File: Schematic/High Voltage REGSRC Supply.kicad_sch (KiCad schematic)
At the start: 10 parts, among them Q17 BSS123

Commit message: added sensors?
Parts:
- renumbered C30 to C32, C31 to C33, C32 to C34, C33 to C35, Q17 to Q21

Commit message: 1st Schematic Review
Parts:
- renumbered C32 to C35, C33 to C36, C34 to C37, C35 to C38, R67 to R69, R68 to R70, R69 to R71, R70 to R72
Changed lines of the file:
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@@
 		(on_board yes)
 		(dnp no)
-		(property "Reference" "#PWR027"
+		(property "Reference" "#PWR032"
 			(at 129.54 104.14 0)
 			(effects
@@
 			(project "STAR"
 				(path "/fc8533bc-25dd-4c20-9b4c-ffebebd6739b/e8da5d81-614b-4fe5-84b3-4c351fab7114/e3d465d4-4bae-42f2-91c8-f61f15aa6ae9"
-					(reference "#PWR027")
+					(reference "#PWR032")
 					(unit 1)
 				)
@@
 		(on_board yes)
 		(dnp no)
-		(property "Reference" "#PWR028"
+		(property "Reference" "#PWR033"
 			(at 152.4 125.73 0)
 			(effects
@@
 			(project "STAR"
 				(path "/fc8533bc-25dd-4c20-9b4c-ffebebd6739b/e8da5d81-614b-4fe5-84b3-4c351fab7114/e3d465d4-4bae-42f2-91c8-f61f15aa6ae9"
-					(reference "#PWR028")
+					(reference "#PWR033")
 					(unit 1)
 				)
@@
 		(on_board yes)
 		(dnp no)
-		(property "Reference" "C33"
+		(property "Reference" "C36"
 			(at 129.54 90.932 0)
 			(effects
@@
 			(project "STAR"
 				(path "/fc8533bc-25dd-4c20-9b4c-ffebebd6739b/e8da5d81-614b-4fe5-84b3-4c351fab7114/e3d465d4-4bae-42f2-91c8-f61f15aa6ae9"
-					(reference "C33")
+					(reference "C36")
 					(unit 1)
 				)
@@
 		(on_board yes)
 		(dnp no)
-		(property "Reference" "R69"
+		(property "Reference" "R71"
 			(at 148.082 81.534 0)
 			(effects
@@
 			(project "STAR"
 				(path "/fc8533bc-25dd-4c20-9b4c-ffebebd6739b/e8da5d81-614b-4fe5-84b3-4c351fab7114/e3d465d4-4bae-42f2-91c8-f61f15aa6ae9"
-					(reference "R69")
+					(reference "R71")
 					(unit 1)
 				)
@@
 		(on_board yes)
 		(dnp no)
-		(property "Reference" "R68"
+		(property "Reference" "R70"
 			(at 144.272 95.504 0)
 			(effects
@@
 			(project "STAR"
 				(path "/fc8533bc-25dd-4c20-9b4c-ffebebd6739b/e8da5d81-614b-4fe5-84b3-4c351fab7114/e3d465d4-4bae-42f2-91c8-f61f15aa6ae9"
-					(reference "R68")
+					(reference "R70")
 					(unit 1)
 				)
@@
 		(on_board yes)
 		(dnp no)
-		(property "Reference" "C32"
+		(property "Reference" "C35"
 			(at 129.54 82.042 0)
 			(effects
@@
 			(project "STAR"
 				(path "/fc8533bc-25dd-4c20-9b4c-ffebebd6739b/e8da5d81-614b-4fe5-84b3-4c351fab7114/e3d465d4-4bae-42f2-91c8-f61f15aa6ae9"
-					(reference "C32")
+					(reference "C35")
 					(unit 1)
 				)
@@
 		(on_board yes)
 		(dnp no)
-		(property "Reference" "C34"
+		(property "Reference" "C37"
 			(at 152.4 112.522 0)
 			(effects
@@
 			(project "STAR"
 				(path "/fc8533bc-25dd-4c20-9b4c-ffebebd6739b/e8da5d81-614b-4fe5-84b3-4c351fab7114/e3d465d4-4bae-42f2-91c8-f61f15aa6ae9"
-					(reference "C34")
+					(reference "C37")
 					(unit 1)
 				)
@@
 		(on_board yes)
 		(dnp no)
-		(property "Reference" "C35"
+		(property "Reference" "C38"
 			(at 161.29 102.362 0)
 			(effects
@@
 			(project "STAR"
 				(path "/fc8533bc-25dd-4c20-9b4c-ffebebd6739b/e8da5d81-614b-4fe5-84b3-4c351fab7114/e3d465d4-4bae-42f2-91c8-f61f15aa6ae9"
-					(reference "C35")
+					(reference "C38")
 					(unit 1)
 				)
@@
 		(on_board yes)
 		(dnp no)
-		(property "Reference" "R70"
+		(property "Reference" "R72"
 			(at 154.432 90.424 0)
 			(effects
@@
 			(project "STAR"
 				(path "/fc8533bc-25dd-4c20-9b4c-ffebebd6739b/e8da5d81-614b-4fe5-84b3-4c351fab7114/e3d465d4-4bae-42f2-91c8-f61f15aa6ae9"
-					(reference "R70")
+					(reference "R72")
 					(unit 1)
 				)
@@
 		(on_board yes)
 		(dnp no)
-		(property "Reference" "R67"
+		(property "Reference" "R69"
 			(at 134.874 78.994 90)
 			(effects
@@
 			(project "STAR"
 				(path "/fc8533bc-25dd-4c20-9b4c-ffebebd6739b/e8da5d81-614b-4fe5-84b3-4c351fab7114/e3d465d4-4bae-42f2-91c8-f61f15aa6ae9"
-					(reference "R67")
+					(reference "R69")
 					(unit 1)
 				)

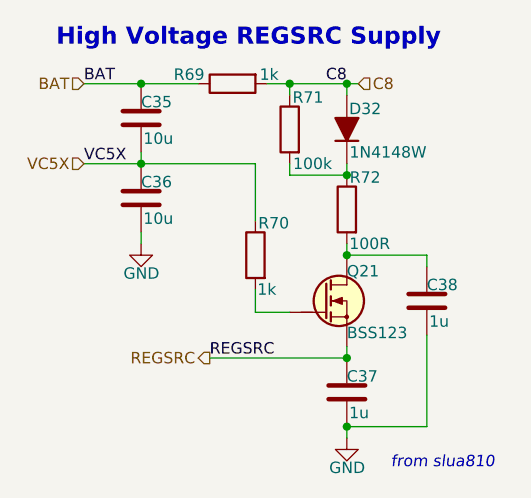
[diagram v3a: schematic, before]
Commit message: Added MCU
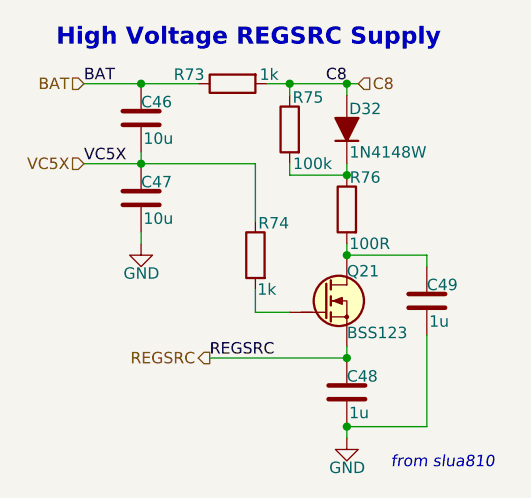
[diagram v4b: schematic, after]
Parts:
- renumbered C35 to C46, C36 to C47, C37 to C48, C38 to C49, R69 to R73, R70 to R74, R71 to R75, R72 to R76
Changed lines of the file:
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@@
 		(on_board yes)
 		(dnp no)
-		(property "Reference" "#PWR033"
+		(property "Reference" "#PWR039"
 			(at 129.54 104.14 0)
 			(effects
@@
 			(project "STAR"
 				(path "/fc8533bc-25dd-4c20-9b4c-ffebebd6739b/e8da5d81-614b-4fe5-84b3-4c351fab7114/e3d465d4-4bae-42f2-91c8-f61f15aa6ae9"
-					(reference "#PWR033")
+					(reference "#PWR039")
 					(unit 1)
 				)
@@
 		(on_board yes)
 		(dnp no)
-		(property "Reference" "#PWR034"
+		(property "Reference" "#PWR040"
 			(at 152.4 125.73 0)
 			(effects
@@
 			(project "STAR"
 				(path "/fc8533bc-25dd-4c20-9b4c-ffebebd6739b/e8da5d81-614b-4fe5-84b3-4c351fab7114/e3d465d4-4bae-42f2-91c8-f61f15aa6ae9"
-					(reference "#PWR034")
+					(reference "#PWR040")
 					(unit 1)
 				)
@@
 		(on_board yes)
 		(dnp no)
-		(property "Reference" "C36"
+		(property "Reference" "C47"
 			(at 129.54 90.932 0)
 			(effects
@@
 			(project "STAR"
 				(path "/fc8533bc-25dd-4c20-9b4c-ffebebd6739b/e8da5d81-614b-4fe5-84b3-4c351fab7114/e3d465d4-4bae-42f2-91c8-f61f15aa6ae9"
-					(reference "C36")
+					(reference "C47")
 					(unit 1)
 				)
@@
 		(on_board yes)
 		(dnp no)
-		(property "Reference" "R71"
+		(property "Reference" "R75"
 			(at 148.082 81.534 0)
 			(effects
@@
 			(project "STAR"
 				(path "/fc8533bc-25dd-4c20-9b4c-ffebebd6739b/e8da5d81-614b-4fe5-84b3-4c351fab7114/e3d465d4-4bae-42f2-91c8-f61f15aa6ae9"
-					(reference "R71")
+					(reference "R75")
 					(unit 1)
 				)
@@
 		(on_board yes)
 		(dnp no)
-		(property "Reference" "R70"
+		(property "Reference" "R74"
 			(at 144.272 95.504 0)
 			(effects
@@
 			(project "STAR"
 				(path "/fc8533bc-25dd-4c20-9b4c-ffebebd6739b/e8da5d81-614b-4fe5-84b3-4c351fab7114/e3d465d4-4bae-42f2-91c8-f61f15aa6ae9"
-					(reference "R70")
+					(reference "R74")
 					(unit 1)
 				)
@@
 		(on_board yes)
 		(dnp no)
-		(property "Reference" "C35"
+		(property "Reference" "C46"
 			(at 129.54 82.042 0)
 			(effects
@@
 			(project "STAR"
 				(path "/fc8533bc-25dd-4c20-9b4c-ffebebd6739b/e8da5d81-614b-4fe5-84b3-4c351fab7114/e3d465d4-4bae-42f2-91c8-f61f15aa6ae9"
-					(reference "C35")
+					(reference "C46")
 					(unit 1)
 				)
@@
 		(on_board yes)
 		(dnp no)
-		(property "Reference" "C37"
+		(property "Reference" "C48"
 			(at 152.4 112.522 0)
 			(effects
@@
 			(project "STAR"
 				(path "/fc8533bc-25dd-4c20-9b4c-ffebebd6739b/e8da5d81-614b-4fe5-84b3-4c351fab7114/e3d465d4-4bae-42f2-91c8-f61f15aa6ae9"
-					(reference "C37")
+					(reference "C48")
 					(unit 1)
 				)
@@
 		(on_board yes)
 		(dnp no)
-		(property "Reference" "C38"
+		(property "Reference" "C49"
 			(at 161.29 102.362 0)
 			(effects
@@
 			(project "STAR"
 				(path "/fc8533bc-25dd-4c20-9b4c-ffebebd6739b/e8da5d81-614b-4fe5-84b3-4c351fab7114/e3d465d4-4bae-42f2-91c8-f61f15aa6ae9"
-					(reference "C38")
+					(reference "C49")
 					(unit 1)
 				)
@@
 		(on_board yes)
 		(dnp no)
-		(property "Reference" "R72"
+		(property "Reference" "R76"
 			(at 154.432 90.424 0)
 			(effects
@@
 			(project "STAR"
 				(path "/fc8533bc-25dd-4c20-9b4c-ffebebd6739b/e8da5d81-614b-4fe5-84b3-4c351fab7114/e3d465d4-4bae-42f2-91c8-f61f15aa6ae9"
-					(reference "R72")
+					(reference "R76")
 					(unit 1)
 				)
@@
 		(on_board yes)
 		(dnp no)
-		(property "Reference" "R69"
+		(property "Reference" "R73"
 			(at 134.874 78.994 90)
 			(effects
@@
 			(project "STAR"
 				(path "/fc8533bc-25dd-4c20-9b4c-ffebebd6739b/e8da5d81-614b-4fe5-84b3-4c351fab7114/e3d465d4-4bae-42f2-91c8-f61f15aa6ae9"
-					(reference "R69")
+					(reference "R73")
 					(unit 1)
 				)

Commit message: Started to work on the BOM
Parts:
- C41: renamed from C46; footprint (none) -> Capacitor_SMD:C_1206_3216Metric_Pad1.33x1.80mm_HandSolder; Link (none) -> https://mou.sr/4l54Mdx; Manufacturer Part Number (none) -> CL31A106KBHNNNE; Price per Unit (none) -> 0.11; Supplier (none) -> Mouser; Supplier Part Number (none) -> 187-CL31A106KBHNNNE
- C42: renamed from C47; footprint (none) -> Capacitor_SMD:C_1206_3216Metric_Pad1.33x1.80mm_HandSolder; Link (none) -> https://mou.sr/4l54Mdx; Manufacturer Part Number (none) -> CL31A106KBHNNNE; Price per Unit (none) -> 0.11; Supplier (none) -> Mouser; Supplier Part Number (none) -> 187-CL31A106KBHNNNE
- C43: renamed from C48; footprint (none) -> Capacitor_SMD:C_1206_3216Metric_Pad1.33x1.80mm_HandSolder; Link (none) -> https://mou.sr/41y0aEA; Manufacturer Part Number (none) -> CL31B105KBHNNNE; Price per Unit (none) -> 0.11; Supplier (none) -> Mouser; Supplier Part Number (none) -> 187-CL31B105KBHNNNE
- C44: renamed from C49; footprint (none) -> Capacitor_SMD:C_1206_3216Metric_Pad1.33x1.80mm_HandSolder; Link (none) -> https://mou.sr/41y0aEA; Manufacturer Part Number (none) -> CL31B105KBHNNNE; Price per Unit (none) -> 0.11; Supplier (none) -> Mouser; Supplier Part Number (none) -> 187-CL31B105KBHNNNE
- D29: renamed from D32; footprint PCM_Diode_SMD_AKL:D_SOD-123 -> 1N4148W:SODFL3816X120N; Link (none) -> https://mou.sr/3kOR7fV; Manufacturer Part Number (none) -> 1N4148W; Price per Unit (none) -> 0.10; Supplier (none) -> Mouser; Supplier Part Number (none) -> 637-1N4148W
- Q21: footprint PCM_Package_TO_SOT_SMD_AKL:SOT-23 -> (none)
- renumbered R73 to R69, R74 to R70, R75 to R71, R76 to R72

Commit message: Massive pivit, simplification
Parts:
- renumbered C41 to C34, C42 to C35, C43 to C36, C44 to C37, D29 to D28
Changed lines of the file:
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@@
 			)
 		)
+		(property "SNAPEDA_PACKAGE_ID" ""
+			(at 149.86 104.14 0)
+			(effects
+				(font
+					(size 1.27 1.27)
+				)
+				(hide yes)
+			)
+		)
 		(pin "1"
 		)
@@
 		(on_board yes)
 		(dnp no)
-		(property "Reference" "#PWR034"
+		(property "Reference" "#PWR023"
 			(at 129.54 104.14 0)
 			(effects
@@
 			(project "STAR"
 				(path "/fc8533bc-25dd-4c20-9b4c-ffebebd6739b/e8da5d81-614b-4fe5-84b3-4c351fab7114/e3d465d4-4bae-42f2-91c8-f61f15aa6ae9"
-					(reference "#PWR034")
+					(reference "#PWR023")
 					(unit 1)
 				)
@@
 		(on_board yes)
 		(dnp no)
-		(property "Reference" "#PWR035"
+		(property "Reference" "#PWR024"
 			(at 152.4 125.73 0)
 			(effects
@@
 			(project "STAR"
 				(path "/fc8533bc-25dd-4c20-9b4c-ffebebd6739b/e8da5d81-614b-4fe5-84b3-4c351fab7114/e3d465d4-4bae-42f2-91c8-f61f15aa6ae9"
-					(reference "#PWR035")
+					(reference "#PWR024")
 					(unit 1)
 				)
@@
 		(on_board yes)
 		(dnp no)
-		(property "Reference" "C42"
+		(property "Reference" "C35"
 			(at 129.54 90.932 0)
 			(effects
@@
 			)
 		)
+		(property "SNAPEDA_PACKAGE_ID" ""
+			(at 129.54 92.71 0)
+			(effects
+				(font
+					(size 1.27 1.27)
+				)
+				(hide yes)
+			)
+		)
 		(pin "1"
 		)
@@
 			(project "STAR"
 				(path "/fc8533bc-25dd-4c20-9b4c-ffebebd6739b/e8da5d81-614b-4fe5-84b3-4c351fab7114/e3d465d4-4bae-42f2-91c8-f61f15aa6ae9"
-					(reference "C42")
+					(reference "C35")
 					(unit 1)
 				)
@@
 			)
 		)
+		(property "SNAPEDA_PACKAGE_ID" ""
+			(at 146.05 85.09 0)
+			(effects
+				(font
+					(size 1.27 1.27)
+				)
+				(hide yes)
+			)
+		)
 		(pin "1"
 		)
@@
 			)
 		)
+		(property "SNAPEDA_PACKAGE_ID" ""
+			(at 142.24 99.06 0)
+			(effects
+				(font
+					(size 1.27 1.27)
+				)
+				(hide yes)
+			)
+		)
 		(pin "1"
 		)
@@
 		(on_board yes)
 		(dnp no)
-		(property "Reference" "C41"
+		(property "Reference" "C34"
 			(at 129.54 82.042 0)
 			(effects
@@
 			)
 		)
+		(property "SNAPEDA_PACKAGE_ID" ""
+			(at 129.54 83.82 0)
+			(effects
+				(font
+					(size 1.27 1.27)
+				)
+				(hide yes)
+			)
+		)
 		(pin "1"
 		)
@@
 			(project "STAR"
 				(path "/fc8533bc-25dd-4c20-9b4c-ffebebd6739b/e8da5d81-614b-4fe5-84b3-4c351fab7114/e3d465d4-4bae-42f2-91c8-f61f15aa6ae9"
-					(reference "C41")
+					(reference "C34")
 					(unit 1)
 				)
@@
 		(on_board yes)
 		(dnp no)
-		(property "Reference" "D29"
+		(property "Reference" "D28"
 			(at 154.432 82.804 90)
 			(effects
@@
 			)
 		)
+		(property "SNAPEDA_PACKAGE_ID" ""
+			(at 152.4 85.09 90)
+			(effects
+				(font
+					(size 1.27 1.27)
+				)
+				(hide yes)
+			)
+		)
 		(pin "2"
 		)
@@
 			(project "STAR"
 				(path "/fc8533bc-25dd-4c20-9b4c-ffebebd6739b/e8da5d81-614b-4fe5-84b3-4c351fab7114/e3d465d4-4bae-42f2-91c8-f61f15aa6ae9"
-					(reference "D29")
+					(reference "D28")
 					(unit 1)
 				)
@@
 		(on_board yes)
 		(dnp no)
-		(property "Reference" "C43"
+		(property "Reference" "C36"
 			(at 152.4 112.522 0)
 			(effects
@@
 			)
 		)
+		(property "SNAPEDA_PACKAGE_ID" ""
+			(at 152.4 114.3 0)
+			(effects
+				(font
+					(size 1.27 1.27)
+				)
+				(hide yes)
+			)
+		)
 		(pin "1"
 		)
@@
 			(project "STAR"
 				(path "/fc8533bc-25dd-4c20-9b4c-ffebebd6739b/e8da5d81-614b-4fe5-84b3-4c351fab7114/e3d465d4-4bae-42f2-91c8-f61f15aa6ae9"
-					(reference "C43")
+					(reference "C36")
 					(unit 1)
 				)
@@
 		(on_board yes)
 		(dnp no)
-		(property "Reference" "C44"
+		(property "Reference" "C37"
 			(at 161.29 102.362 0)
 			(effects
@@
 			)
 		)
+		(property "SNAPEDA_PACKAGE_ID" ""
+			(at 161.29 104.14 0)
+			(effects
+				(font
+					(size 1.27 1.27)
+				)
+				(hide yes)
+			)
+		)
 		(pin "1"
 		)
@@
 			(project "STAR"
 				(path "/fc8533bc-25dd-4c20-9b4c-ffebebd6739b/e8da5d81-614b-4fe5-84b3-4c351fab7114/e3d465d4-4bae-42f2-91c8-f61f15aa6ae9"
-					(reference "C44")
+					(reference "C37")
 					(unit 1)
 				)
@@
 			)
 		)
+		(property "SNAPEDA_PACKAGE_ID" ""
+			(at 152.4 93.98 0)
+			(effects
+				(font
+					(size 1.27 1.27)
+				)
+				(hide yes)
+			)
+		)
 		(pin "1"
 		)
@@
 			(at 139.7 80.01 90)
 			(effects
+				(font
+					(size 1.27 1.27)
+				)
+				(hide yes)
+			)
+		)
+		(property "SNAPEDA_PACKAGE_ID" ""
+			(at 139.7 80.01 90)
+			(effects
